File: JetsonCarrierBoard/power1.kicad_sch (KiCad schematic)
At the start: 0 parts

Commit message: Adding voltage divider for correct VOUT
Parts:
- added R?: 73k, symbol Device:R
- added R?: 10k, symbol Device:R
- added U?: SIC43x, symbol Voltage_Regulators_Switching:SIC43x
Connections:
- new net: R?.1, R?.2, U?.17 (FB)
- new net: R?.1, U?.18 (VOUT)
- new net +BATT: U?.1 (VIN), U?.2 (VIN), U?.22 (VIN), U?.26 (VIN)
- new net GND: R?.2, U?.13 (PGND), U?.16 (AGND), U?.25 (AGND), U?.27 (PGND), U?.3 (PGND), U?.4 (PGND)
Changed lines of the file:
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@@
 (kicad_sch (version 20211123) (generator eeschema)
   (paper "A4")
+  (junction (at 161.29 115.57) (diameter 0) (color 0 0 0 0)
+  )
+  (junction (at 130.81 120.65) (diameter 0) (color 0 0 0 0)
+  )
+  (junction (at 130.81 83.82) (diameter 0) (color 0 0 0 0)
+  )
+  (junction (at 130.81 81.28) (diameter 0) (color 0 0 0 0)
+  )
+  (junction (at 130.81 86.36) (diameter 0) (color 0 0 0 0)
+  )
+  (junction (at 161.29 118.11) (diameter 0) (color 0 0 0 0)
+  )
+  (junction (at 168.91 109.22) (diameter 0) (color 0 0 0 0)
+  )
+  (junction (at 161.29 120.65) (diameter 0) (color 0 0 0 0)
+  )
+  (wire (pts (xy 161.29 113.03) (xy 158.75 113.03))
+    (stroke (width 0) (type default) (color 0 0 0 0))
+  )
+  (wire (pts (xy 130.81 86.36) (xy 133.35 86.36))
+    (stroke (width 0) (type default) (color 0 0 0 0))
+  )
+  (wire (pts (xy 130.81 81.28) (xy 130.81 78.74))
+    (stroke (width 0) (type default) (color 0 0 0 0))
+  )
+  (wire (pts (xy 130.81 81.28) (xy 133.35 81.28))
+    (stroke (width 0) (type default) (color 0 0 0 0))
+  )
+  (wire (pts (xy 130.81 88.9) (xy 130.81 86.36))
+    (stroke (width 0) (type default) (color 0 0 0 0))
+  )
+  (wire (pts (xy 161.29 118.11) (xy 161.29 115.57))
+    (stroke (width 0) (type default) (color 0 0 0 0))
+  )
+  (wire (pts (xy 133.35 88.9) (xy 130.81 88.9))
+    (stroke (width 0) (type default) (color 0 0 0 0))
+  )
+  (wire (pts (xy 168.91 109.22) (xy 158.75 109.22))
+    (stroke (width 0) (type default) (color 0 0 0 0))
+  )
+  (wire (pts (xy 168.91 109.22) (xy 168.91 110.49))
+    (stroke (width 0) (type default) (color 0 0 0 0))
+  )
+  (wire (pts (xy 130.81 86.36) (xy 130.81 83.82))
+    (stroke (width 0) (type default) (color 0 0 0 0))
+  )
+  (wire (pts (xy 168.91 120.65) (xy 161.29 120.65))
+    (stroke (width 0) (type default) (color 0 0 0 0))
+  )
+  (wire (pts (xy 158.75 115.57) (xy 161.29 115.57))
+    (stroke (width 0) (type default) (color 0 0 0 0))
+  )
+  (wire (pts (xy 161.29 120.65) (xy 161.29 123.19))
+    (stroke (width 0) (type default) (color 0 0 0 0))
+  )
+  (wire (pts (xy 130.81 83.82) (xy 133.35 83.82))
+    (stroke (width 0) (type default) (color 0 0 0 0))
+  )
+  (wire (pts (xy 130.81 83.82) (xy 130.81 81.28))
+    (stroke (width 0) (type default) (color 0 0 0 0))
+  )
+  (wire (pts (xy 161.29 120.65) (xy 161.29 118.11))
+    (stroke (width 0) (type default) (color 0 0 0 0))
+  )
+  (wire (pts (xy 161.29 115.57) (xy 161.29 113.03))
+    (stroke (width 0) (type default) (color 0 0 0 0))
+  )
+  (wire (pts (xy 158.75 120.65) (xy 161.29 120.65))
+    (stroke (width 0) (type default) (color 0 0 0 0))
+  )
+  (wire (pts (xy 133.35 120.65) (xy 130.81 120.65))
+    (stroke (width 0) (type default) (color 0 0 0 0))
+  )
+  (wire (pts (xy 158.75 118.11) (xy 161.29 118.11))
+    (stroke (width 0) (type default) (color 0 0 0 0))
+  )
+  (wire (pts (xy 133.35 118.11) (xy 130.81 118.11))
+    (stroke (width 0) (type default) (color 0 0 0 0))
+  )
+  (wire (pts (xy 168.91 105.41) (xy 168.91 109.22))
+    (stroke (width 0) (type default) (color 0 0 0 0))
+  )
+  (wire (pts (xy 130.81 120.65) (xy 130.81 123.19))
+    (stroke (width 0) (type default) (color 0 0 0 0))
+  )
+  (wire (pts (xy 130.81 118.11) (xy 130.81 120.65))
+    (stroke (width 0) (type default) (color 0 0 0 0))
+  )
+  (wire (pts (xy 158.75 105.41) (xy 161.29 105.41))
+    (stroke (width 0) (type default) (color 0 0 0 0))
+  )
+  (wire (pts (xy 168.91 118.11) (xy 168.91 120.65))
+    (stroke (width 0) (type default) (color 0 0 0 0))
+  )
+  (symbol (lib_id "Voltage_Regulators_Switching:SIC43x") (at 146.05 80.01 0) (unit 1)
+    (in_bom yes) (on_board yes) (fields_autoplaced)
+    (property "Reference" "U?" (id 0) (at 146.05 73.66 0))
+    (property "Value" "SIC43x" (id 1) (at 146.05 76.2 0))
+    (property "Footprint" "" (id 2) (at 151.13 80.01 0)
+      (effects (font (size 1.27 1.27)) hide)
+    )
+    (property "Datasheet" "" (id 3) (at 151.13 80.01 0)
+      (effects (font (size 1.27 1.27)) hide)
+    )
+    (pin "1")
+    (pin "10")
+    (pin "11")
+    (pin "12")
+    (pin "13")
+    (pin "14")
+    (pin "15")
+    (pin "16")
+    (pin "17")
+    (pin "18")
+    (pin "19")
+    (pin "2")
+    (pin "20")
+    (pin "21")
+    (pin "22")
+    (pin "23")
+    (pin "24")
+    (pin "25")
+    (pin "26")
+    (pin "27")
+    (pin "28")
+    (pin "3")
+    (pin "4")
+    (pin "5")
+    (pin "6")
+    (pin "7")
+    (pin "8")
+    (pin "9")
+  )
+  (symbol (lib_id "power:GND") (at 130.81 123.19 0) (unit 1)
+    (in_bom yes) (on_board yes) (fields_autoplaced)
+    (property "Reference" "#PWR?" (id 0) (at 130.81 129.54 0)
+      (effects (font (size 1.27 1.27)) hide)
+    )
+    (property "Value" "GND" (id 1) (at 130.81 128.27 0))
+    (property "Footprint" "" (id 2) (at 130.81 123.19 0)
+      (effects (font (size 1.27 1.27)) hide)
+    )
+    (property "Datasheet" "" (id 3) (at 130.81 123.19 0)
+      (effects (font (size 1.27 1.27)) hide)
+    )
+    (pin "1")
+  )
+  (symbol (lib_id "Device:R") (at 165.1 105.41 90) (unit 1)
+    (in_bom yes) (on_board yes)
+    (property "Reference" "R?" (id 0) (at 162.56 102.87 90))
+    (property "Value" "73k" (id 1) (at 166.37 102.87 90))
+    (property "Footprint" "" (id 2) (at 165.1 107.188 90)
+      (effects (font (size 1.27 1.27)) hide)
+    )
+    (property "Datasheet" "~" (id 3) (at 165.1 105.41 0)
+      (effects (font (size 1.27 1.27)) hide)
+    )
+    (pin "1")
+    (pin "2")
+  )
+  (symbol (lib_id "power:+BATT") (at 130.81 78.74 0) (unit 1)
+    (in_bom yes) (on_board yes) (fields_autoplaced)
+    (property "Reference" "#PWR?" (id 0) (at 130.81 82.55 0)
+      (effects (font (size 1.27 1.27)) hide)
+    )
+    (property "Value" "+BATT" (id 1) (at 130.81 73.66 0))
+    (property "Footprint" "" (id 2) (at 130.81 78.74 0)
+      (effects (font (size 1.27 1.27)) hide)
+    )
+    (property "Datasheet" "" (id 3) (at 130.81 78.74 0)
+      (effects (font (size 1.27 1.27)) hide)
+    )
+    (pin "1")
+  )
+  (symbol (lib_id "power:GND") (at 161.29 123.19 0) (unit 1)
+    (in_bom yes) (on_board yes) (fields_autoplaced)
+    (property "Reference" "#PWR?" (id 0) (at 161.29 129.54 0)
+      (effects (font (size 1.27 1.27)) hide)
+    )
+    (property "Value" "GND" (id 1) (at 161.29 128.27 0))
+    (property "Footprint" "" (id 2) (at 161.29 123.19 0)
+      (effects (font (size 1.27 1.27)) hide)
+    )
+    (property "Datasheet" "" (id 3) (at 161.29 123.19 0)
+      (effects (font (size 1.27 1.27)) hide)
+    )
+    (pin "1")
+  )
+  (symbol (lib_id "Device:R") (at 168.91 114.3 0) (unit 1)
+    (in_bom yes) (on_board yes) (fields_autoplaced)
+    (property "Reference" "R?" (id 0) (at 171.45 113.0299 0)
+      (effects (font (size 1.27 1.27)) (justify left))
+    )
+    (property "Value" "10k" (id 1) (at 171.45 115.5699 0)
+      (effects (font (size 1.27 1.27)) (justify left))
+    )
+    (property "Footprint" "" (id 2) (at 167.132 114.3 90)
+      (effects (font (size 1.27 1.27)) hide)
+    )
+    (property "Datasheet" "~" (id 3) (at 168.91 114.3 0)
+      (effects (font (size 1.27 1.27)) hide)
+    )
+    (pin "1")
+    (pin "2")
+  )
 )

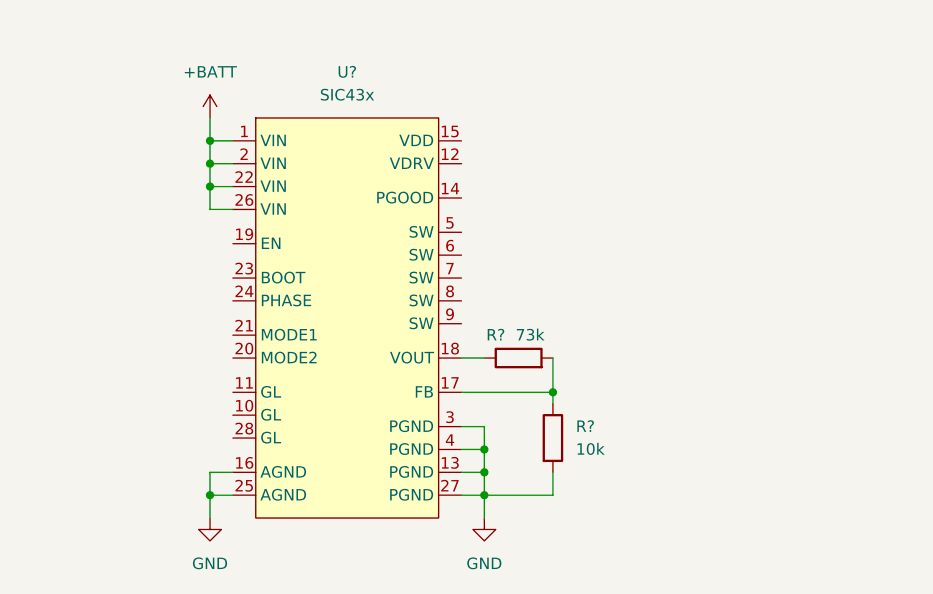
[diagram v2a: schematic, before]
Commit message: Buck 5V temp done
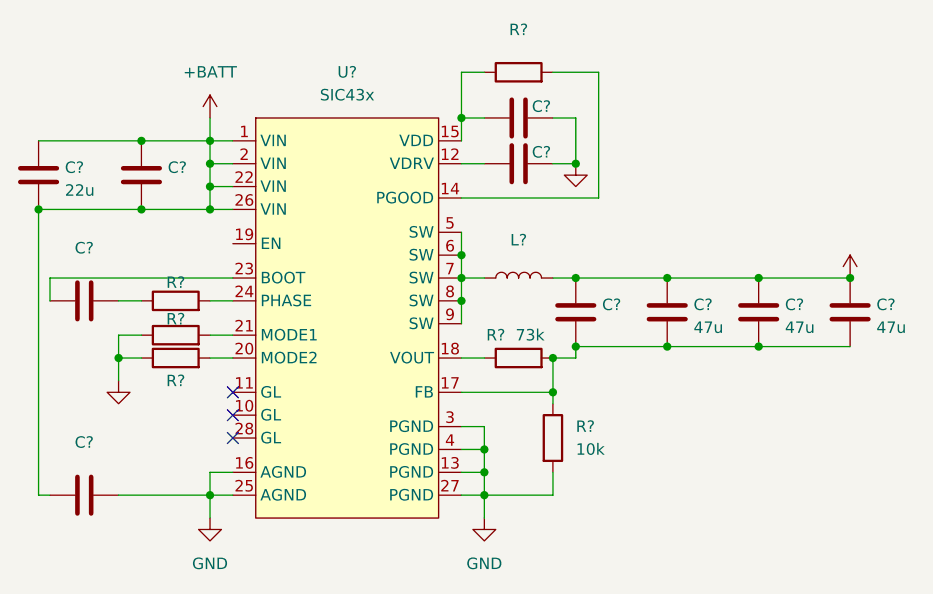
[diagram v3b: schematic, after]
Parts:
- added C? (x6): (no value), symbol Device:C
- added C? (x3): 47u, symbol Device:C
- added C?: 22u, symbol Device:C
- added L?: (no value), symbol Device:L
- added R? (x4): (no value), symbol Device:R
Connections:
- net +BATT: now also C?.1, C?.1, C?.1, C?.2, C?.2
- net GND: now also C?.2, C?.2, C?.2, R?.1, R?.1
- net at U?.12 (VDRV): now also C?.1
- net at U?.14 (PGOOD): now also R?.2
- net at U?.15 (VDD): now also C?.1, R?.1
- net at R?.1, R?.2, U?.17 (FB): now also C?.2, C?.2, C?.2, C?.2
- net at U?.20 (MODE2): now also R?.2
- net at U?.21 (MODE1): now also R?.2
- net at U?.23 (BOOT): now also C?.1
- net at U?.24 (PHASE): now also R?.2
- net at U?.5 (SW): now also U?.6 (SW), U?.7 (SW), U?.8 (SW), U?.9 (SW), L?.1
- new net: C?.2, R?.1
- new net +5V: C?.1, C?.1, C?.1, C?.1, L?.2
- no-connect marks 0 -> 3

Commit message: Update 3.3V and 1.8V Power + Mic
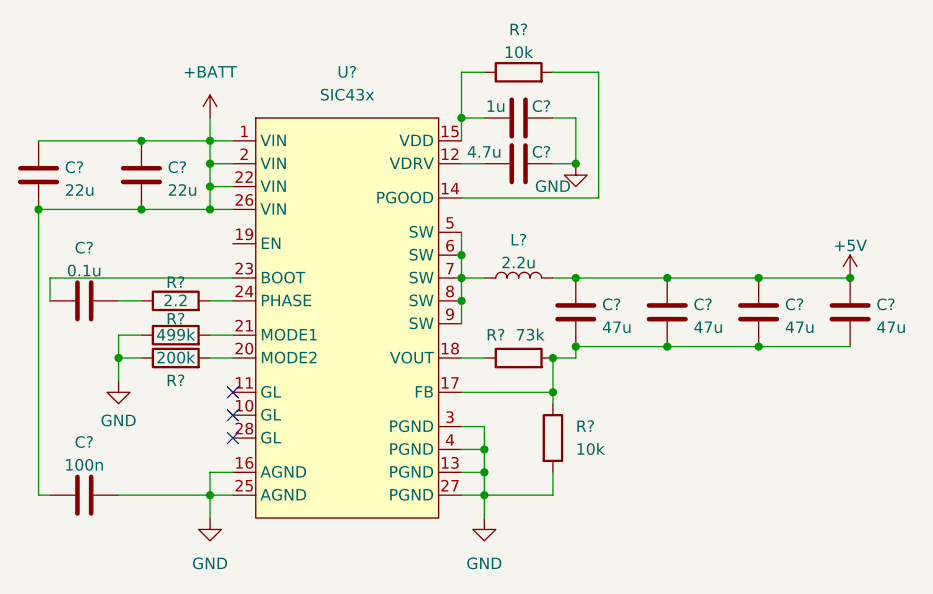
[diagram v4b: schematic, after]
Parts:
- C?: value (none) -> 1u
- C?: value (none) -> 4.7u
- C?: value (none) -> 0.1u
- C?: value (none) -> 47u
- C?: value (none) -> 22u
- C?: value (none) -> 100n
- L?: value (none) -> 2.2u
- R?: value (none) -> 2.2
- R?: value (none) -> 10k
- R?: value (none) -> 200k
- R?: value (none) -> 499k
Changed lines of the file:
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@@
     (in_bom yes) (on_board yes)
     (property "Reference" "C?" (id 0) (at 167.64 77.47 90))
-    (property "Value" "" (id 1) (at 162.56 77.47 90))
+    (property "Value" "1u" (id 1) (at 162.56 77.47 90))
     (property "Footprint" "" (id 2) (at 168.91 77.7748 0)
       (effects (font (size 1.27 1.27)) hide)
@@
     (in_bom yes) (on_board yes)
     (property "Reference" "C?" (id 0) (at 167.64 82.55 90))
-    (property "Value" "" (id 1) (at 161.29 82.55 90))
+    (property "Value" "4.7u" (id 1) (at 161.29 82.55 90))
     (property "Footprint" "" (id 2) (at 168.91 82.8548 0)
       (effects (font (size 1.27 1.27)) hide)
@@
     (in_bom yes) (on_board yes)
     (property "Reference" "R?" (id 0) (at 127 97.028 90))
-    (property "Value" "" (id 1) (at 127 99.06 90))
+    (property "Value" "2.2" (id 1) (at 127 99.06 90))
     (property "Footprint" "" (id 2) (at 127 100.838 90)
       (effects (font (size 1.27 1.27)) hide)
@@
     (in_bom yes) (on_board yes) (fields_autoplaced)
     (property "Reference" "L?" (id 0) (at 165.1 92.3122 90))
-    (property "Value" "" (id 1) (at 165.1 94.8491 90))
+    (property "Value" "2.2u" (id 1) (at 165.1 94.8491 90))
     (property "Footprint" "" (id 2) (at 165.1 96.52 0)
       (effects (font (size 1.27 1.27)) hide)
@@
     (in_bom yes) (on_board yes) (fields_autoplaced)
     (property "Reference" "R?" (id 0) (at 165.1 68.9442 90))
-    (property "Value" "" (id 1) (at 165.1 71.4811 90))
+    (property "Value" "10k" (id 1) (at 165.1 71.4811 90))
     (property "Footprint" "" (id 2) (at 165.1 75.438 90)
       (effects (font (size 1.27 1.27)) hide)
@@
     (in_bom yes) (on_board yes) (fields_autoplaced)
     (property "Reference" "C?" (id 0) (at 116.84 93.2012 90))
-    (property "Value" "" (id 1) (at 116.84 95.7381 90))
+    (property "Value" "0.1u" (id 1) (at 116.84 95.7381 90))
     (property "Footprint" "" (id 2) (at 120.65 98.0948 0)
       (effects (font (size 1.27 1.27)) hide)
@@
       (effects (font (size 1.27 1.27)) (justify left))
     )
-    (property "Value" "" (id 1) (at 174.371 102.0322 0)
+    (property "Value" "47u" (id 1) (at 174.371 102.0322 0)
       (effects (font (size 1.27 1.27)) (justify left))
     )
@@
       (effects (font (size 1.27 1.27)) hide)
     )
-    (property "Value" "" (id 1) (at 201.93 92.9442 0))
+    (property "Value" "+5V" (id 1) (at 201.93 92.9442 0))
     (property "Footprint" "" (id 2) (at 201.93 96.52 0)
       (effects (font (size 1.27 1.27)) hide)
@@
     (in_bom yes) (on_board yes)
     (property "Reference" "R?" (id 0) (at 127 107.95 90))
-    (property "Value" "" (id 1) (at 127 105.41 90))
+    (property "Value" "200k" (id 1) (at 127 105.41 90))
     (property "Footprint" "" (id 2) (at 127 107.188 90)
       (effects (font (size 1.27 1.27)) hide)
@@
       (effects (font (size 1.27 1.27)) (justify left))
     )
-    (property "Value" "" (id 1) (at 126.111 86.7922 0)
+    (property "Value" "22u" (id 1) (at 126.111 86.7922 0)
       (effects (font (size 1.27 1.27)) (justify left))
     )
@@
       (effects (font (size 1.27 1.27)) hide)
     )
-    (property "Value" "" (id 1) (at 168.91 86.36 0))
+    (property "Value" "GND" (id 1) (at 168.91 86.36 0))
     (property "Footprint" "" (id 2) (at 171.45 83.82 0)
       (effects (font (size 1.27 1.27)) hide)
@@
     (in_bom yes) (on_board yes) (fields_autoplaced)
     (property "Reference" "C?" (id 0) (at 116.84 114.7912 90))
-    (property "Value" "" (id 1) (at 116.84 117.3281 90))
+    (property "Value" "100n" (id 1) (at 116.84 117.3281 90))
     (property "Footprint" "" (id 2) (at 120.65 119.6848 0)
       (effects (font (size 1.27 1.27)) hide)
@@
       (effects (font (size 1.27 1.27)) hide)
     )
-    (property "Value" "" (id 1) (at 120.65 112.3934 0))
+    (property "Value" "GND" (id 1) (at 120.65 112.3934 0))
     (property "Footprint" "" (id 2) (at 120.65 107.95 0)
       (effects (font (size 1.27 1.27)) hide)
@@
     (in_bom yes) (on_board yes)
     (property "Reference" "R?" (id 0) (at 127 101.092 90))
-    (property "Value" "" (id 1) (at 127 102.87 90))
+    (property "Value" "499k" (id 1) (at 127 102.87 90))
     (property "Footprint" "" (id 2) (at 127 104.648 90)
       (effects (font (size 1.27 1.27)) hide)
